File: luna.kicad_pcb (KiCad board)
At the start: 2 copper layers, 85 x 60 mm, 21 parts, among them J1 Conn_01x06_Male, J2 Conn_02x10_Top_Bottom, J3 Conn_01x02_Male, J4 Conn_01x02_Male, J5 Conn_01x02_Male, J6 Conn_01x02_Male, Q1 2N7002, Q2 2N7002, Q3 2N7002, Q4 2N7002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

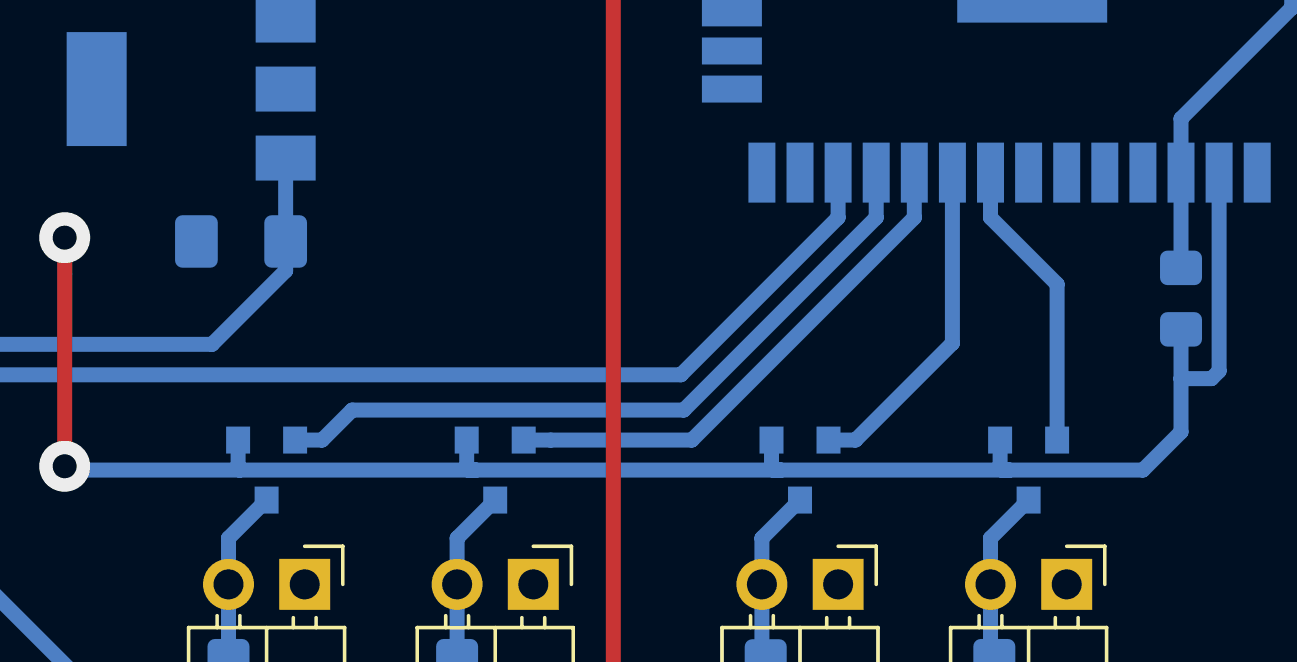
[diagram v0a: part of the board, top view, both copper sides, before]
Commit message: Added output pin descriptions.
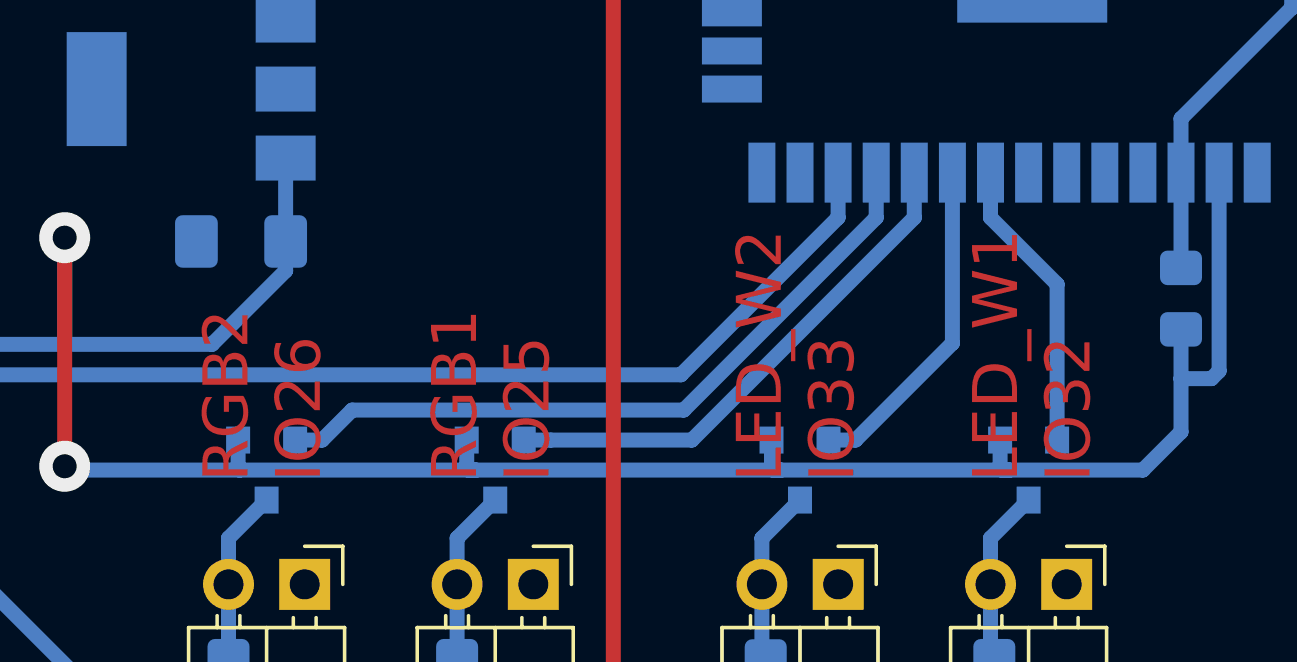
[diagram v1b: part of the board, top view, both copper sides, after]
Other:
- board text added: "LED_W1 IO32"
- board text added: "LED_W2 IO33"
- board text added: "RGB1 IO25"
- board text added: "RGB2 IO26"
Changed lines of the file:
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@@
   (general
     (thickness 1.6)
-    (drawings 4)
+    (drawings 8)
     (tracks 132)
     (zones 0)
@@
     (solder_mask_min_width 0.25)
     (aux_axis_origin 0 0)
-    (visible_elements FFFFFF7F)
+    (visible_elements 7FFFFFFF)
     (pcbplotparams
       (layerselection 0x010fc_ffffffff)
@@
     )
   )
+  (gr_text "RGB2\nIO26" (at 43.688 45.466 90) (layer F.Cu)
+    (effects (font (size 1.5 1.5) (thickness 0.3)) (justify left))
+  )
+  (gr_text "RGB1\nIO25" (at 51.308 45.466 90) (layer F.Cu)
+    (effects (font (size 1.5 1.5) (thickness 0.3)) (justify left))
+  )
+  (gr_text "LED_W2\nIO33" (at 61.468 45.466 90) (layer F.Cu)
+    (effects (font (size 1.5 1.5) (thickness 0.3)) (justify left))
+  )
+  (gr_text "LED_W1\nIO32" (at 69.342 45.466 90) (layer F.Cu)
+    (effects (font (size 1.5 1.5) (thickness 0.3)) (justify left))
+  )
   (gr_line (start 0 60) (end 0 0) (layer Edge.Cuts) (width 0.05))

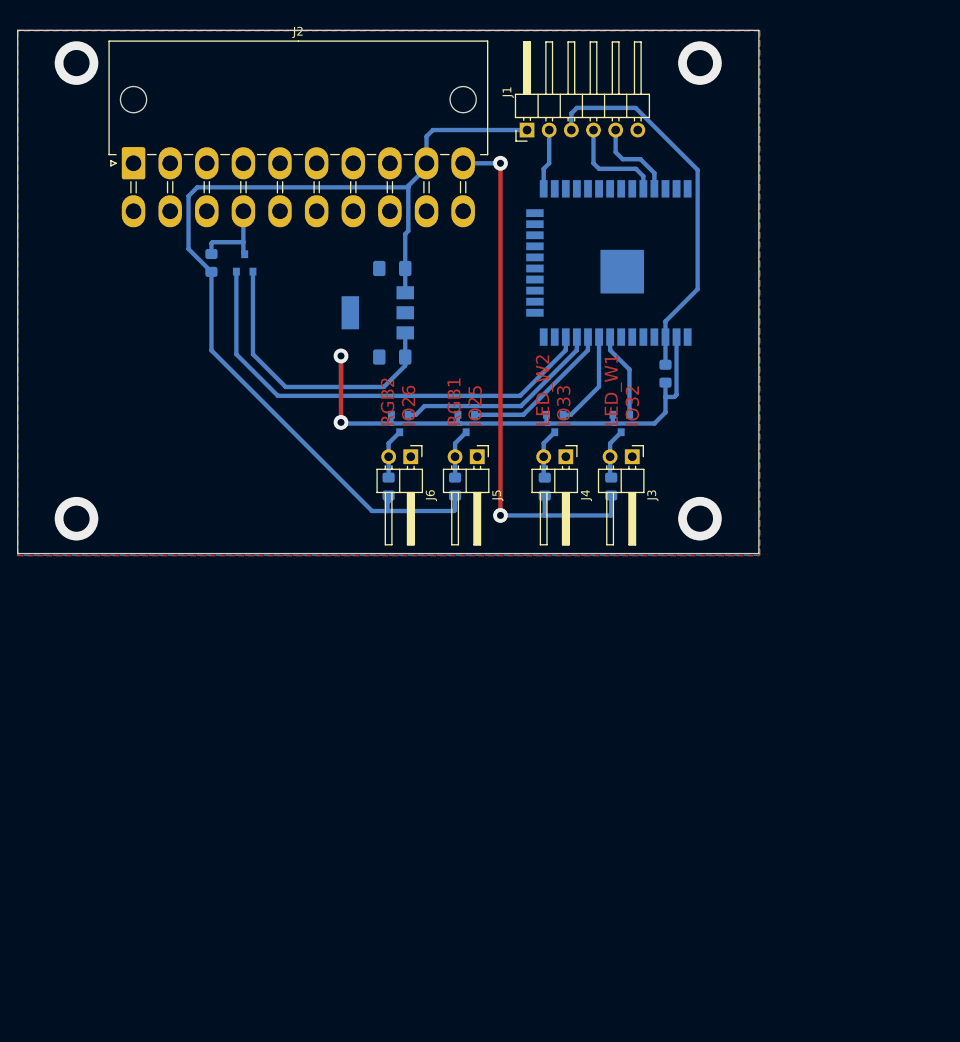
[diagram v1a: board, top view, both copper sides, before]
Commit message: Second revision with on-board led swithes and dummy load output.
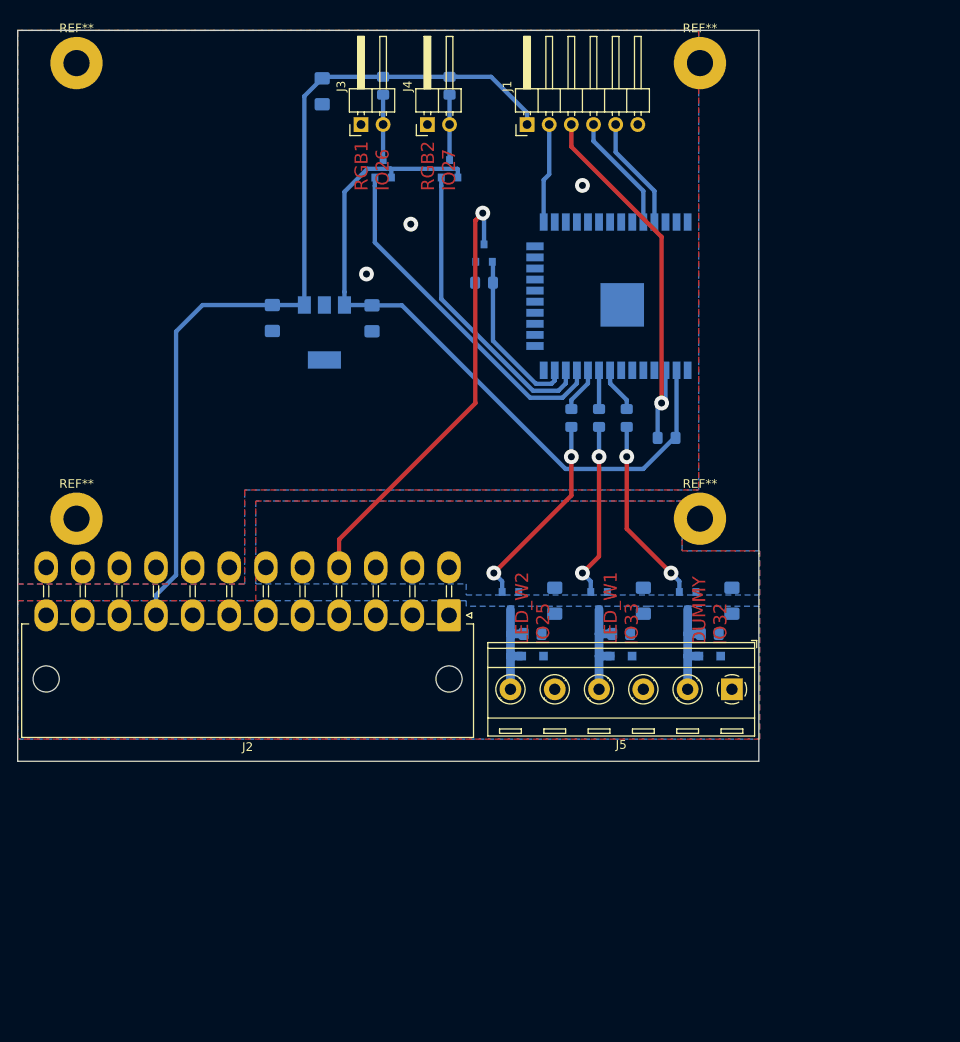
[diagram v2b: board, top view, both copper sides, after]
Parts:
- removed J6: Conn_01x02_Male, Connector_PinHeader_2.54mm:PinHeader_1x02_P2.54mm_Horizontal
- added C3: 10u, Capacitor_SMD:C_1206_3216Metric_Pad1.42x1.75mm_HandSolder, B.Cu at (40.6, 33.0)
- added C4: 10u, Capacitor_SMD:C_1206_3216Metric_Pad1.42x1.75mm_HandSolder, B.Cu at (61.6, 65.4)
- added C5: 10u, Capacitor_SMD:C_1206_3216Metric_Pad1.42x1.75mm_HandSolder, B.Cu at (71.8, 65.4)
- added C6: 10u, Capacitor_SMD:C_1206_3216Metric_Pad1.42x1.75mm_HandSolder, B.Cu at (81.9, 65.4)
- added D1: D_Schottky, Diode_SMD:D_SOD-323_HandSoldering, B.Cu at (79.4, 71.8)
- added D2: D_Schottky, Diode_SMD:D_SOD-323_HandSoldering, B.Cu at (69.2, 71.8)
- added D3: D_Schottky, Diode_SMD:D_SOD-323_HandSoldering, B.Cu at (59.1, 71.8)
- added Q6: DMN3404L, Package_TO_SOT_SMD:SOT-23, B.Cu at (56.5, 65.4)
- added R10: 10k, Resistor_SMD:R_0805_2012Metric_Pad1.15x1.40mm_HandSolder, B.Cu at (59.1, 69.2)
- added R7: 100, Resistor_SMD:R_0805_2012Metric_Pad1.15x1.40mm_HandSolder, B.Cu at (63.5, 44.5)
- added R8: 10k, Resistor_SMD:R_0805_2012Metric_Pad1.15x1.40mm_HandSolder, B.Cu at (79.4, 69.2)
- added R9: 10k, Resistor_SMD:R_0805_2012Metric_Pad1.15x1.40mm_HandSolder, B.Cu at (69.2, 69.2)
- added REF**: MountingHole_3mm_Pad, MountingHole:MountingHole_3mm_Pad, F.Cu at (6.75, 56.0)
- added REF**: MountingHole_3mm_Pad, MountingHole:MountingHole_3mm_Pad, F.Cu at (78.2, 56.0)
- added REF**: MountingHole_3mm_Pad, MountingHole:MountingHole_3mm_Pad, F.Cu at (6.75, 3.75)
- added REF**: MountingHole_3mm_Pad, MountingHole:MountingHole_3mm_Pad, F.Cu at (78.2, 3.75)
- J2: value Conn_02x10_Top_Bottom -> Conn_02x12_Top_Bottom; footprint Connector_Molex:Molex_Mini-Fit_Jr_5569-20A2_2x10_P4.20mm_Horizontal -> Connector_Molex:Molex_Mini-Fit_Jr_5569-24A2_2x12_P4.20mm_Horizontal
- J5: value Conn_01x02_Male -> Screw_Terminal_01x06; footprint Connector_PinHeader_2.54mm:PinHeader_1x02_P2.54mm_Horizontal -> TerminalBlock_RND:TerminalBlock_RND_205-00291_1x06_P5.08mm_Horizontal
- Q4, Q5: value 2N7002 -> DMN3404L
- R1: value 10k -> 1k
- R4: value 1k -> 10k
- R5, R6: value 10k -> 100
- moved J2 63.2 mm to (49.5, 67.1), turned to 180 degrees
- moved R3 49.6 mm to (49.5, 6.35), turned to 270 degrees
- moved J3 49.2 mm to (39.4, 10.8), turned to 90 degrees
- moved J4 41.3 mm to (47.0, 10.8), turned to 90 degrees
- moved J5 39.6 mm to (81.9, 75.6), turned to 180 degrees
- moved Q4 32.5 mm to (76.8, 65.4)
- moved Q3 31.6 mm to (49.5, 15.9), turned to 90 degrees
- moved Q5 30.6 mm to (66.7, 65.4)
- moved R1 28.3 mm to (41.9, 6.35), turned to 270 degrees
- moved R6 25.4 mm to (66.7, 44.5), turned to 270 degrees
- moved Q2 25.1 mm to (53.5, 25.5), turned to 90 degrees
- moved R2 23.3 mm to (53.5, 28.9), turned to 180 degrees
- moved C1 21.9 mm to (34.9, 6.99), turned to 270 degrees
- moved R5 21.2 mm to (69.8, 44.5), turned to 270 degrees
- moved Q1 19.2 mm to (41.9, 15.9)
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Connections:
- C1 pad 1: GND -> +5V
- C1 pad 2: +5V -> GND
- C2 pad 1: VDD -> GND
- C2 pad 2: GND -> +5V
- J2 pad 11: Net-(J2-Pad11) -> +12V
- J2 pad 17: Net-(J2-Pad17) -> GNDPWR
- J2 pad 18: Net-(J2-Pad18) -> GNDPWR
- J2 pad 19: Net-(J2-Pad19) -> GND
- J2 pad 7: GND -> Net-(J2-Pad7)
- J5 pad 1: GND -> +12V
- J5 pad 2: Net-(J5-Pad2) -> DUMMY_LOAD_OUT
- Q1 pad 2: ~ON~ -> RGB1
- Q1 pad 3: Net-(J2-Pad14) -> Net-(J3-Pad2)
- Q2 pad 1: VDD -> ~ON~
- Q2 pad 2: LED_W1 -> GND
- Q2 pad 3: Net-(J3-Pad2) -> Net-(J2-Pad16)
- Q3 pad 2: LED_W2 -> RGB2
- Q4 pad 1: VDD -> Net-(Q4-Pad1)
- Q4 pad 2: RGB1 -> GNDPWR
- Q4 pad 3: Net-(J5-Pad2) -> DUMMY_LOAD_OUT
- Q5 pad 1: VDD -> Net-(Q5-Pad1)
- Q5 pad 2: RGB2 -> GNDPWR
- Q5 pad 3: Net-(J6-Pad2) -> LED_W1_OUT
- R1 pad 2: Net-(J2-Pad14) -> Net-(J3-Pad2)
- R2 pad 1: VDD -> ~ON~
- R2 pad 2: EN -> GND
- R3 pad 1: +12V -> +5V
- R3 pad 2: Net-(J3-Pad2) -> Net-(J4-Pad2)
- R4 pad 1: +12V -> VDD
- R4 pad 2: Net-(J4-Pad2) -> EN
- R5 pad 1: +5V -> DUMMY_LOAD
- R5 pad 2: Net-(J5-Pad2) -> Net-(Q4-Pad1)
- R6 pad 1: +5V -> LED_W1
- R6 pad 2: Net-(J6-Pad2) -> Net-(Q5-Pad1)
- U2 pad 10: RGB1 -> LED_W2
- U2 pad 11: RGB2 -> RGB1
- U2 pad 12: ~ON~ -> RGB2
- U2 pad 13: Net-(U2-Pad13) -> ~ON~
- U2 pad 8: LED_W1 -> DUMMY_LOAD
- U2 pad 9: LED_W2 -> LED_W1
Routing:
- net +12V: track 61.9 -> 0.00 mm, vias 2 -> 0
- net Net-(J2-Pad16): track 0.00 -> 51.1 mm, vias 0 -> 1
- net ~ON~: track 52.9 -> 19.5 mm
- net Net-(Q6-Pad1): track 0.00 -> 23.0 mm, vias 0 -> 2
- net RGB1: track 17.6 -> 40.2 mm
- net Net-(Q4-Pad1): track 0.00 -> 21.4 mm, vias 0 -> 2
- net Net-(Q5-Pad1): track 0.00 -> 20.1 mm, vias 0 -> 2
- net VDD: track 98.5 -> 84.4 mm, vias 2 -> 0
- net LED_W1_OUT: track 0.00 -> 12.0 mm
- net DUMMY_LOAD_OUT: track 0.00 -> 12.0 mm
- net LED_W2_OUT: track 0.00 -> 12.0 mm
- net +5V: track 114.3 -> 102.9 mm
- net RGB2: track 23.9 -> 34.4 mm
- net Net-(J2-Pad14): track 9.93 -> 0.00 mm
- net LED_W2: track 11.2 -> 5.23 mm
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- added copper zone on B.Cu, net +12V
- added copper zone on B.Cu, net GNDPWR
- added copper zone on F.Cu, net GNDPWR
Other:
- board size 85 x 60 mm -> 85 x 83.8 mm
- board text added: "DUMMY IO32"
- board text added: "LED_W1 IO33"
- board text added: "LED_W2 IO25"
- board text added: "RGB1 IO26"
- board text added: "RGB2 IO27"
- board text removed: "LED_W1 IO32"
- board text removed: "LED_W2 IO33"
- board text removed: "RGB1 IO25"
- board text removed: "RGB2 IO26"

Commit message: Changed voltage regulator to LD1117. Added mounting holes to schematic. Removed flyback diode and resistor from dummy driver. Removed gate resistors.
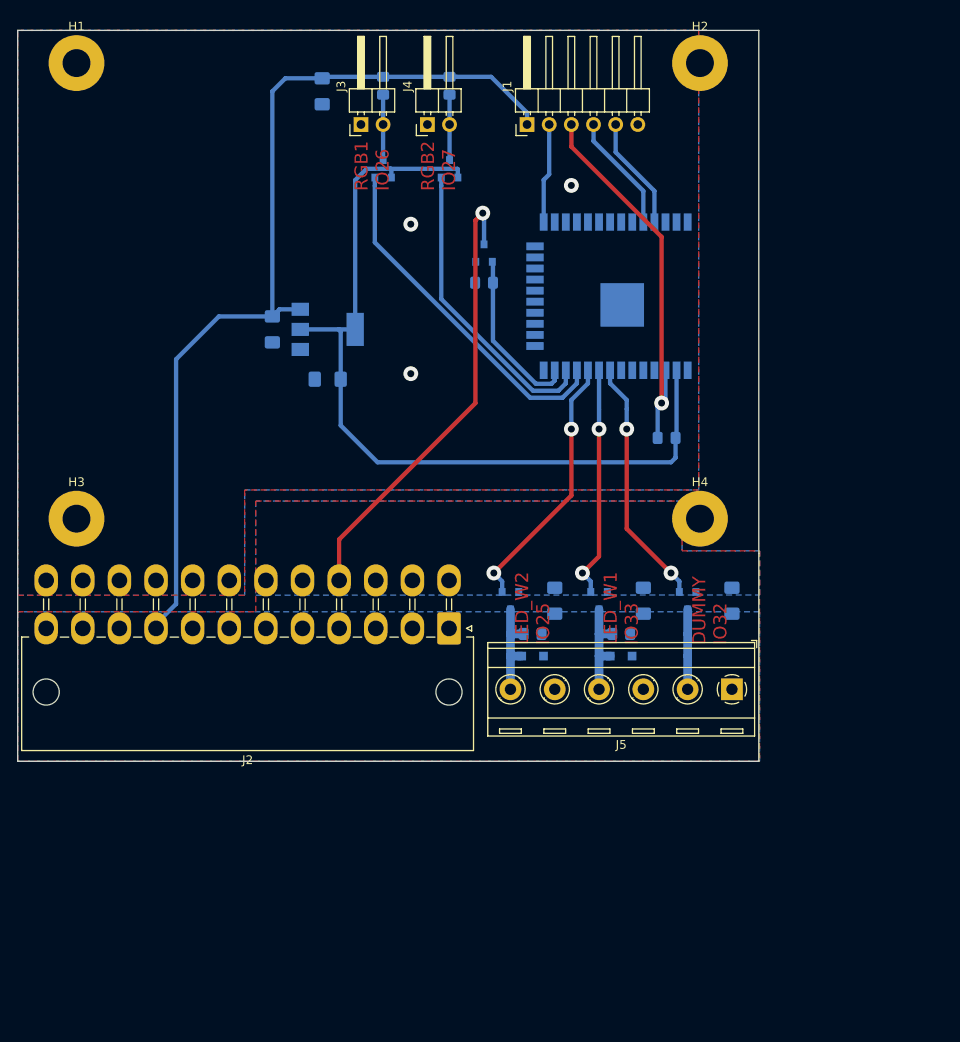
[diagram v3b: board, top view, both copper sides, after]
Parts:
- removed D3: D_Schottky, Diode_SMD:D_SOD-323_HandSoldering
- removed R10, R8, R9: 10k, Resistor_SMD:R_0805_2012Metric_Pad1.15x1.40mm_HandSolder
- removed R7: 100, Resistor_SMD:R_0805_2012Metric_Pad1.15x1.40mm_HandSolder
- removed REF** (x4): MountingHole_3mm_Pad, MountingHole:MountingHole_3mm_Pad
- added H1: MountingHole_Pad, MountingHole:MountingHole_3.2mm_M3_Pad, F.Cu at (6.75, 3.75)
- added H2: MountingHole_Pad, MountingHole:MountingHole_3.2mm_M3_Pad, F.Cu at (78.2, 3.75)
- added H3: MountingHole_Pad, MountingHole:MountingHole_3.2mm_M3_Pad, F.Cu at (6.75, 56.0)
- added H4: MountingHole_Pad, MountingHole:MountingHole_3.2mm_M3_Pad, F.Cu at (78.2, 56.0)
- R5, R6: value 100 -> 10k
- U1: value LM2936-3.3 -> LD1117S33TR_SOT223
- moved R6 25.9 mm to (59.1, 69.2), turned to 180 degrees
- moved R5 24.8 mm to (69.2, 69.2), turned to 180 degrees
- moved D2 10.2 mm to (59.1, 71.8)
- moved D1 10.2 mm to (69.2, 71.8)
- moved C3 8.64 mm to (35.6, 40.0), turned to 180 degrees
- moved J2 1.50 mm to (49.5, 68.6)
- moved C2 1.31 mm to (29.2, 34.3)
- moved U1 0.52 mm to (35.6, 34.3), turned to 0 degrees
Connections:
- D1 pad 2: DUMMY_LOAD_OUT -> LED_W1_OUT
- D2 pad 2: LED_W1_OUT -> LED_W2_OUT
- Q4 pad 1: Net-(Q4-Pad1) -> DUMMY_LOAD
- Q5 pad 1: Net-(Q5-Pad1) -> LED_W1
- Q6 pad 1: Net-(Q6-Pad1) -> LED_W2
- R5 pad 1: DUMMY_LOAD -> +12V
- R5 pad 2: Net-(Q4-Pad1) -> LED_W1_OUT
- R6 pad 1: LED_W1 -> +12V
- R6 pad 2: Net-(Q5-Pad1) -> LED_W2_OUT
- U1 pad 1: +5V -> GND
- U1 pad 2: GND -> VDD
- U1 pad 3: VDD -> +5V
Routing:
- net LED_W2: track 5.23 -> 30.3 mm, vias 0 -> 2
- net DUMMY_LOAD: track 5.23 -> 28.7 mm, vias 0 -> 2
- net Net-(Q6-Pad1): track 23.0 -> 0.00 mm, vias 2 -> 0
- net LED_W1: track 4.45 -> 26.6 mm, vias 0 -> 2
- net Net-(Q4-Pad1): track 21.4 -> 0.00 mm, vias 2 -> 0
- net Net-(Q5-Pad1): track 20.1 -> 0.00 mm, vias 2 -> 0
- net VDD: track 84.4 -> 99.5 mm
- net +5V: track 102.9 -> 107.2 mm
- net DUMMY_LOAD_OUT: track 12.0 -> 9.16 mm
